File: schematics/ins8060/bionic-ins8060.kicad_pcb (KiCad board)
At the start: 2 copper layers, 48.3 x 71.1 mm, 9 parts, among them J1 Bionic-P135, J2 Bionic-P245, U1 INS8060, U3 11AA010-I/TO

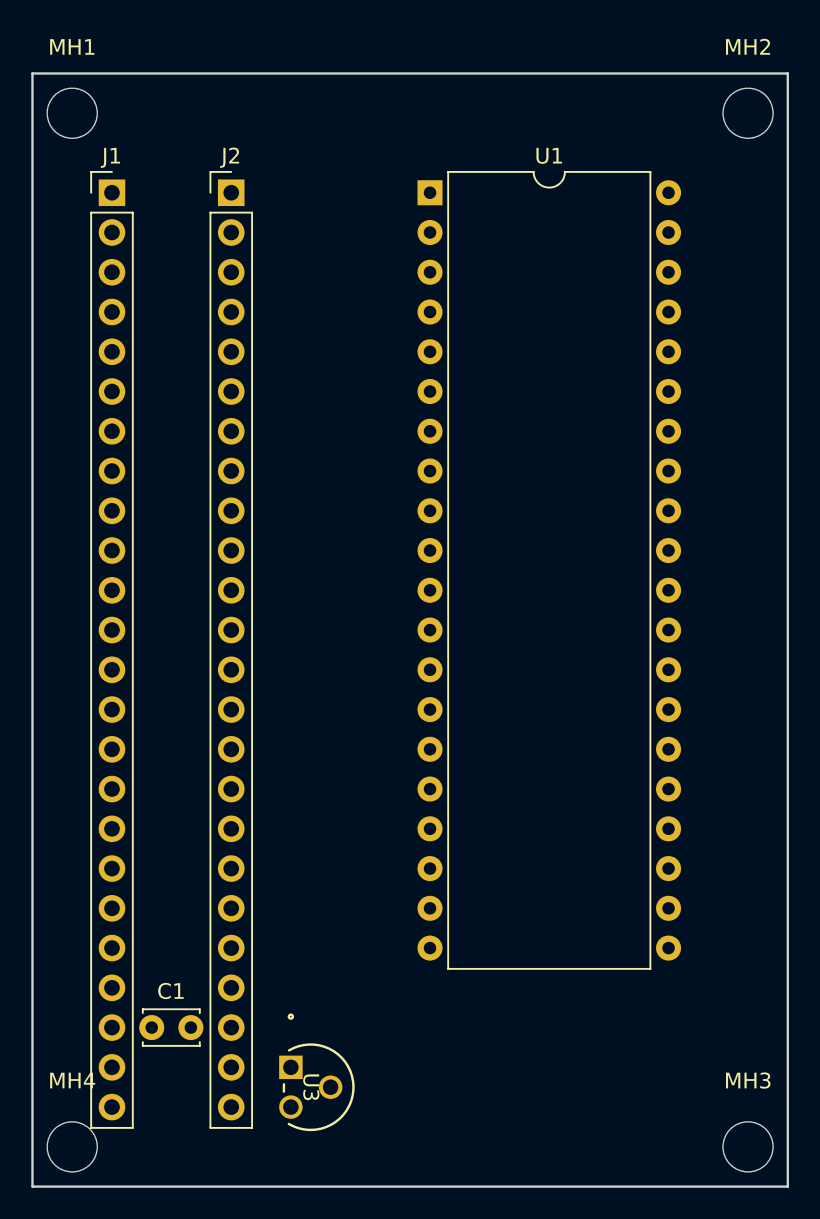
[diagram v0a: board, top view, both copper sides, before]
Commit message: [INS8060] Add power LED
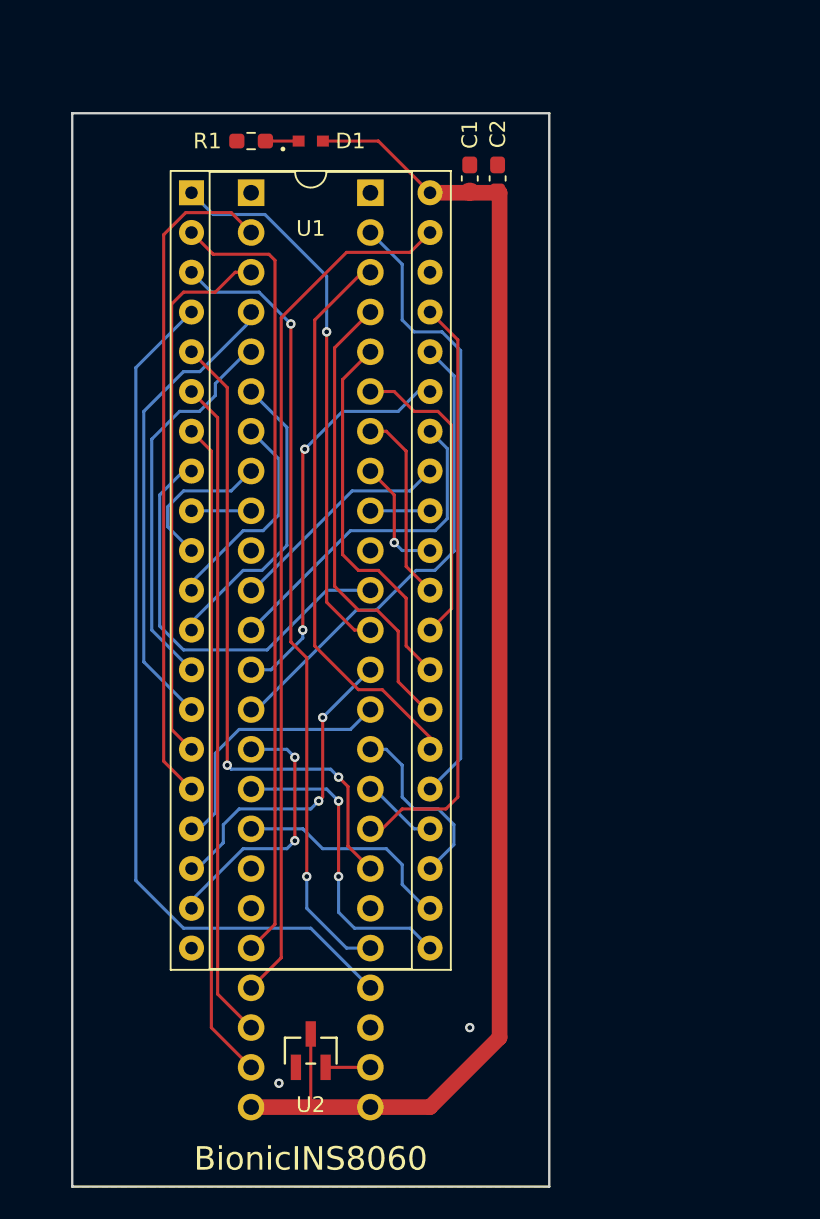
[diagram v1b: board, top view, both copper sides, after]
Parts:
- removed MH1, MH2, MH3, MH4: MountingHole_3.2mm_M3, MountingHole:MountingHole_3.2mm_M3
- removed U3: 11AA010-I/TO, microchip:TO-92_MC_MCH
- added C2: 22u, Capacitor_SMD:C_0603_1608Metric_Pad1.08x0.95mm_HandSolder, F.Cu at (128.2, 74.2)
- added D1: CSL1901UW1, 0-LocalLibrary:LED_CSL1901UW1_ROM, F.Cu at (116.2, 71.8)
- added R1: 1.6k, Resistor_SMD:R_0603_1608Metric_Pad0.98x0.95mm_HandSolder, F.Cu at (112.4, 71.8)
- added U2: 11AA010-I/TT, 0-LocalLibrary:SOT-23_MC_MCH-M, F.Cu at (116.2, 129.9)
- C1: footprint Capacitor_THT:C_Disc_D3.4mm_W2.1mm_P2.50mm -> Capacitor_SMD:C_0603_1608Metric_Pad1.08x0.95mm_HandSolder
- J1: footprint connector:Bionic-P135_Vertical -> 0-LocalLibrary:Bionic-P135_Vertical; moved to B.Cu
- J2: footprint connector:Bionic-P245_Vertical -> 0-LocalLibrary:Bionic-P245_Vertical; moved to B.Cu
- U1: footprint Package_DIP:DIP-40_W15.24mm -> 0-LocalLibrary:DIP-40_W15.24mm_Socket
- moved C1 57.9 mm to (126.4, 74.2), turned to 90 degrees
- moved U1 15.2 mm to (108.6, 75.1)
- moved J1 8.89 mm to (112.4, 75.1), turned to 180 degrees
- moved J2 8.89 mm to (120.0, 75.1), turned to 180 degrees
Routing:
- net VCC: track 0.00 -> 89.4 mm
- net /P55: track 0.00 -> 55.6 mm
- net /P51: track 0.00 -> 55.4 mm
- net /P50: track 0.00 -> 50.9 mm
- net /P54: track 0.00 -> 50.6 mm, vias 0 -> 2
- net /P10: track 0.00 -> 42.9 mm
- net /P53: track 0.00 -> 42.2 mm
- net /P52: track 0.00 -> 42.2 mm
- net /P47: track 0.00 -> 41.5 mm, vias 0 -> 2
- net /P20: track 0.00 -> 39.8 mm
- net /P46: track 0.00 -> 38.2 mm
- net /P21: track 0.00 -> 36.2 mm
- net /P11: track 0.00 -> 36.0 mm
- net /P41: track 0.00 -> 35.2 mm, vias 0 -> 1
- net /P33: track 0.00 -> 30.5 mm
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- added copper zone on B.Cu, net GND
- added copper zone on F.Cu, net GND
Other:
- board size 48.3 x 71.1 mm -> 30.5 x 68.6 mm
- board text added: "BionicINS8060"
- board text added: "Rev. 5"

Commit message: [schematics] Make board edges round
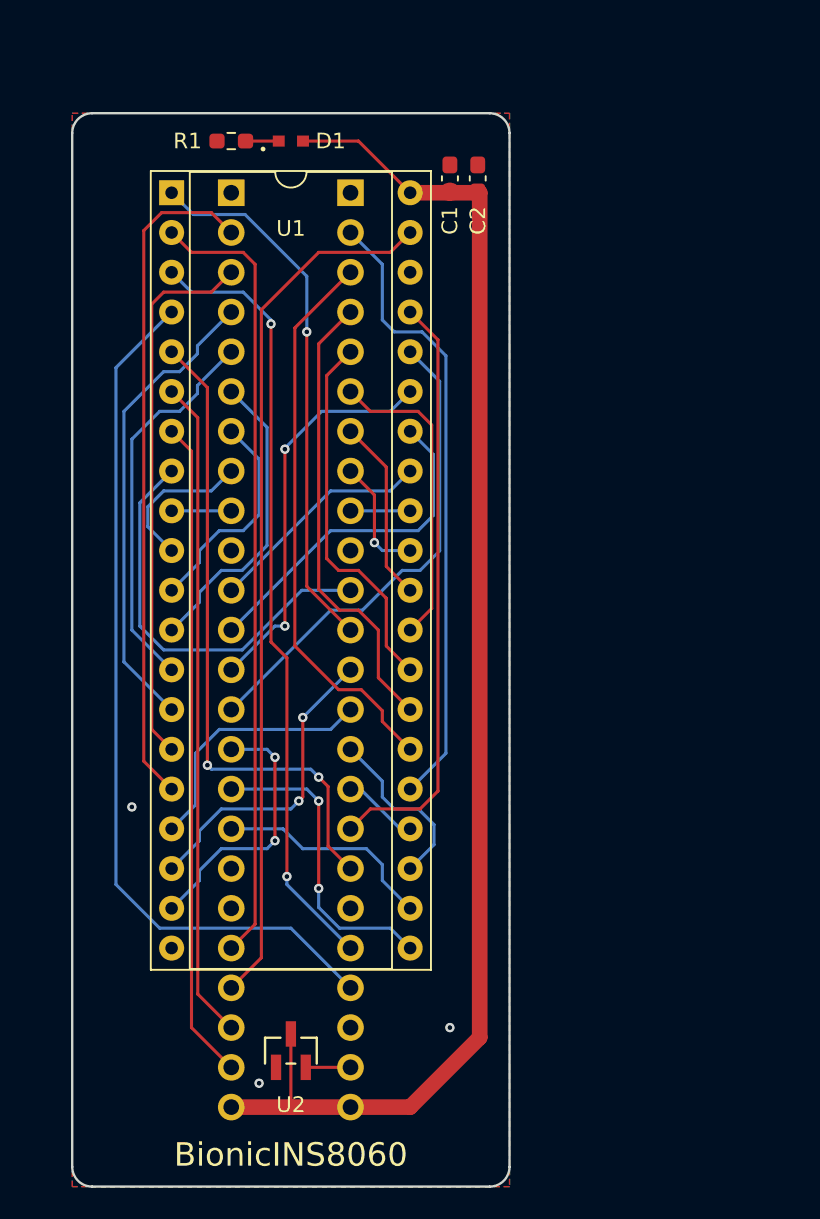
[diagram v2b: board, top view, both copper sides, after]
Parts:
- moved C1 1.27 mm to (125.1, 74.2)
- moved J1 1.27 mm to (111.2, 75.1)
- moved R1 1.27 mm to (111.2, 71.8)
- moved U1 1.27 mm to (107.3, 75.1)
- moved C2 1.27 mm to (126.9, 74.2)
- moved D1 1.27 mm to (115.0, 71.8)
- moved J2 1.27 mm to (118.8, 75.1)
- moved U2 1.27 mm to (115.0, 129.9)
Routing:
- net /P54: track 50.6 -> 49.8 mm
- net /P44: track 12.0 -> 11.4 mm
- net /P25: track 12.3 -> 11.7 mm
- net /P41: track 35.2 -> 34.6 mm
- net GND: vias 2 -> 3
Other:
- board size 30.5 x 68.6 mm -> 27.9 x 68.6 mm
- board text added: "JLCJLCJLCJLC"

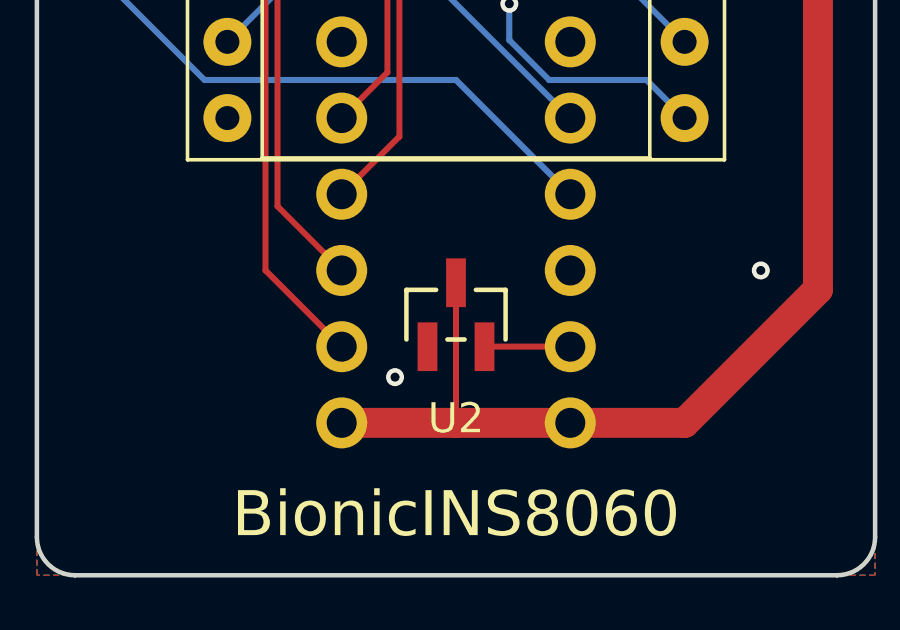
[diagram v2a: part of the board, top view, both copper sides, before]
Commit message: [INS8060] Fix EEPROM pinout
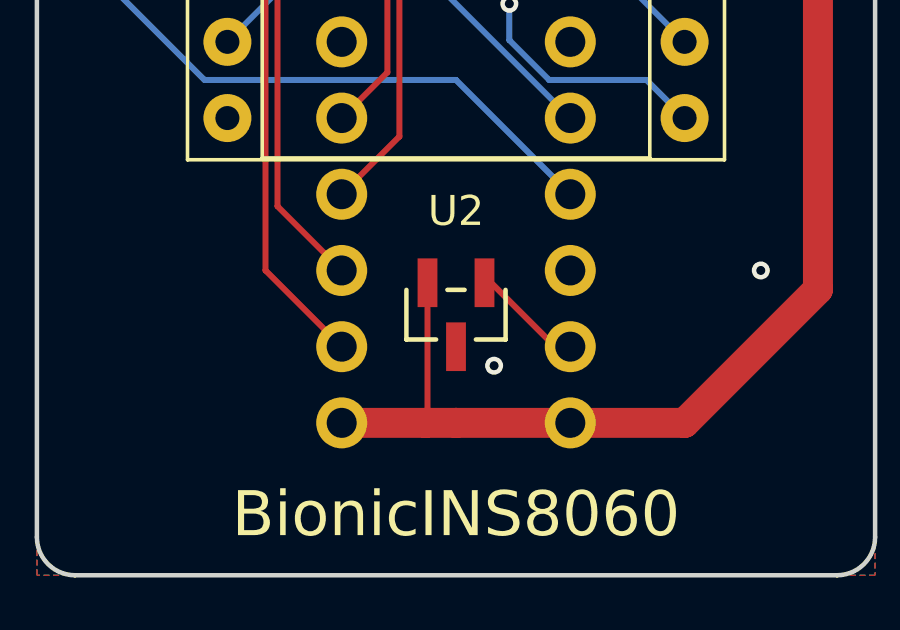
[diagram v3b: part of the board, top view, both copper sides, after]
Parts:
- turned U2 to 180 degrees
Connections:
- U2 pad 1: GND -> Net-(J2-P57)
- U2 pad 2: Net-(J2-P57) -> VCC
- U2 pad 3: VCC -> GND
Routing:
- net Net-(J2-P57): track 2.94 -> 3.74 mm
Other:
- board text added: "Rev. 6"
- board text removed: "Rev. 5"
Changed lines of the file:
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@@
   (title_block
     (title "BionicINS8060")
-    (date "2024-04-24")
-    (rev "5")
+    (date "2024-11-01")
+    (rev "6")
     (company "Tadashi G. Takaoka")
   )
@@
   )
   (footprint "0-LocalLibrary:SOT-23_MC_MCH-M" (layer "F.Cu")
-    (at 114.97 129.894)
+    (at 114.97 129.894 180)
     (descr "Microchip 11AAxxx-I/TT UNI/O 1Kbit Serial EEPROM")
     (property "Sheetfile" "bionic-ins8060.kicad_sch")
@@
         (effects (font (size 1 1) (thickness 0.15)))
     )
-    (fp_text value "11AA010-I/TT" (at 0 0 unlocked) (layer "F.Fab")
+    (fp_text value "11AA010-I/TT" (at 0 0 180 unlocked) (layer "F.Fab")
         (effects (font (size 1 1) (thickness 0.15)))
     )
-    (fp_text user "${REFERENCE}" (at 0 0 unlocked) (layer "F.Fab")
+    (fp_text user "${REFERENCE}" (at 0 0 180 unlocked) (layer "F.Fab")
         (effects (font (size 1 1) (thickness 0.15)))
     )
@@
     (fp_circle (center -1.270999 0.446) (end -1.143999 0.446)
       (stroke (width 0.0254) (type solid)) (fill none) (layer "F.Fab"))
-    (pad "1" smd rect (at -0.950001 1.066) (size 0.6604 1.6256) (layers "F.Cu" "F.Paste" "F.Mask")
+    (pad "1" smd rect (at -0.950001 1.066 180) (size 0.6604 1.6256) (layers "F.Cu" "F.Paste" "F.Mask")
+      (net 43 "Net-(J2-P57)") (pinfunction "SCIO") (pintype "bidirectional"))
+    (pad "2" smd rect (at 0.950001 1.066 180) (size 0.6604 1.6256) (layers "F.Cu" "F.Paste" "F.Mask")
+      (net 1 "VCC") (pinfunction "VCC") (pintype "power_in"))
+    (pad "3" smd rect (at 0 -1.066 180) (size 0.6604 1.6256) (layers "F.Cu" "F.Paste" "F.Mask")
       (net 2 "GND") (pinfunction "VSS") (pintype "power_in"))
-    (pad "2" smd rect (at 0.950001 1.066) (size 0.6604 1.6256) (layers "F.Cu" "F.Paste" "F.Mask")
-      (net 43 "Net-(J2-P57)") (pinfunction "SCIO") (pintype "bidirectional"))
-    (pad "3" smd rect (at 0 -1.066) (size 0.6604 1.6256) (layers "F.Cu" "F.Paste" "F.Mask")
-      (net 1 "VCC") (pinfunction "VCC") (pintype "power_in"))
     (model "${KIPRJMOD}/0-LocalLibrary/SOT-23_MC_MCH.step"
       (offset (xyz 0 0 0))
@@
   (gr_arc (start 102.27 138.58) (mid 101.371974 138.208026) (end 101 137.31)
     (stroke (width 0.15) (type default)) (layer "Edge.Cuts"))
-  (gr_text "Rev. 5" (at 107.096 136.802) (layer "B.SilkS")
+  (gr_text "Rev. 6" (at 107.096 136.802) (layer "B.SilkS")
     (effects (font (size 1 1)) (justify left mirror))
   )
@@
   (segment (start 122.59 133.5) (end 127.035 129.055) (width 1) (layer "F.Cu") (net 1))
   (segment (start 114.97 133.5) (end 118.78 133.5) (width 1) (layer "F.Cu") (net 1))
+  (segment (start 114.019999 128.828) (end 114.019999 133.434001) (width 0.2) (layer "F.Cu") (net 1))
   (segment (start 125.13 75.08) (end 122.59 75.08) (width 1) (layer "F.Cu") (net 1))
-  (segment (start 111.16 133.5) (end 114.97 133.5) (width 1) (layer "F.Cu") (net 1))
-  (segment (start 114.97 133.5) (end 114.97 128.624) (width 0.2) (layer "F.Cu") (net 1))
+  (segment (start 114.019999 133.434001) (end 113.954 133.5) (width 0.2) (layer "F.Cu") (net 1))
   (segment (start 118.78 133.5) (end 122.59 133.5) (width 1) (layer "F.Cu") (net 1))
   (segment (start 125.13 75.08) (end 125.13 74.9265) (width 1) (layer "F.Cu") (net 1))
   (segment (start 119.288 71.778) (end 122.59 75.08) (width 0.2) (layer "F.Cu") (net 1))
+  (segment (start 111.16 133.5) (end 113.954 133.5) (width 1) (layer "F.Cu") (net 1))
   (segment (start 115.7447 71.778) (end 119.288 71.778) (width 0.2) (layer "F.Cu") (net 1))
   (segment (start 127.035 75.08) (end 125.13 75.08) (width 1) (layer "F.Cu") (net 1))
+  (segment (start 113.954 133.5) (end 114.97 133.5) (width 1) (layer "F.Cu") (net 1))
   (segment (start 127.035 129.055) (end 127.035 75.08) (width 1) (layer "F.Cu") (net 1))
-  (via (at 112.938 131.976) (size 0.6) (drill 0.3) (layers "F.Cu" "B.Cu") (free) (net 2))
   (via (at 125.13 128.42) (size 0.6) (drill 0.3) (layers "F.Cu" "B.Cu") (free) (net 2))
+  (via (at 116.24 131.595) (size 0.6) (drill 0.3) (layers "F.Cu" "B.Cu") (free) (net 2))
   (via (at 104.81 114.323) (size 0.6) (drill 0.3) (layers "F.Cu" "B.Cu") (free) (net 2))
   (segment (start 108.62 91.59) (end 107.35 90.32) (width 0.2) (layer "F.Cu") (net 3))
@@
   (segment (start 107.35 77.62) (end 108.62 78.89) (width 0.2) (layer "F.Cu") (net 39))
   (segment (start 112.684 121.816) (end 111.16 123.34) (width 0.2) (layer "F.Cu") (net 39))
-  (segment (start 118.78 130.96) (end 116.124 130.96) (width 0.2) (layer "F.Cu") (net 43))
-  (segment (start 116.124 130.96) (end 115.92 130.756) (width 0.2) (layer "F.Cu") (net 43))
+  (segment (start 116.14 128.828) (end 118.272 130.96) (width 0.2) (layer "F.Cu") (net 43))
+  (segment (start 118.272 130.96) (end 118.78 130.96) (width 0.2) (layer "F.Cu") (net 43))
+  (segment (start 115.920001 128.828) (end 116.14 128.828) (width 0.2) (layer "F.Cu") (net 43))
   (segment (start 114.1953 71.778) (end 112.0725 71.778) (width 0.2) (layer "F.Cu") (net 48))
   (zone (net 2) (net_name "GND") (layers "F&B.Cu") (hatch edge 0.5)

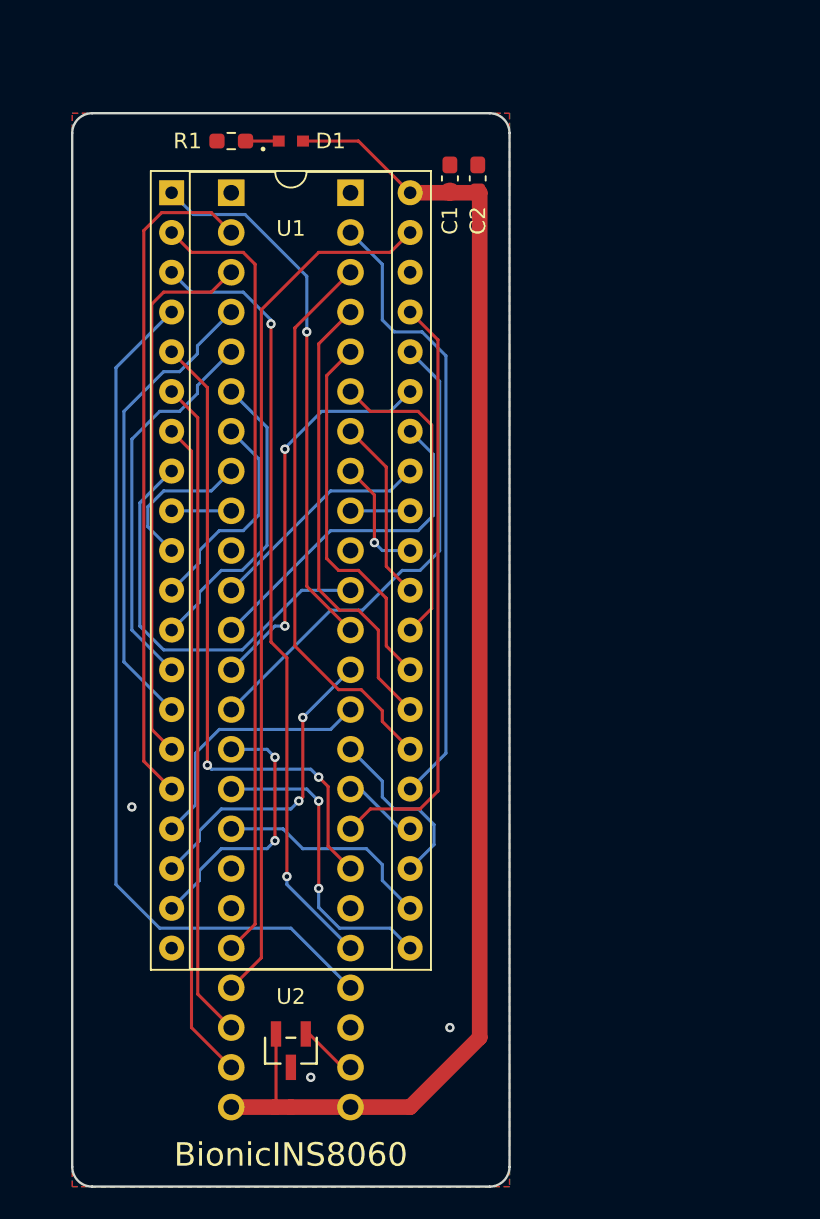
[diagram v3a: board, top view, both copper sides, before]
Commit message: [INS8060] Shrink board size
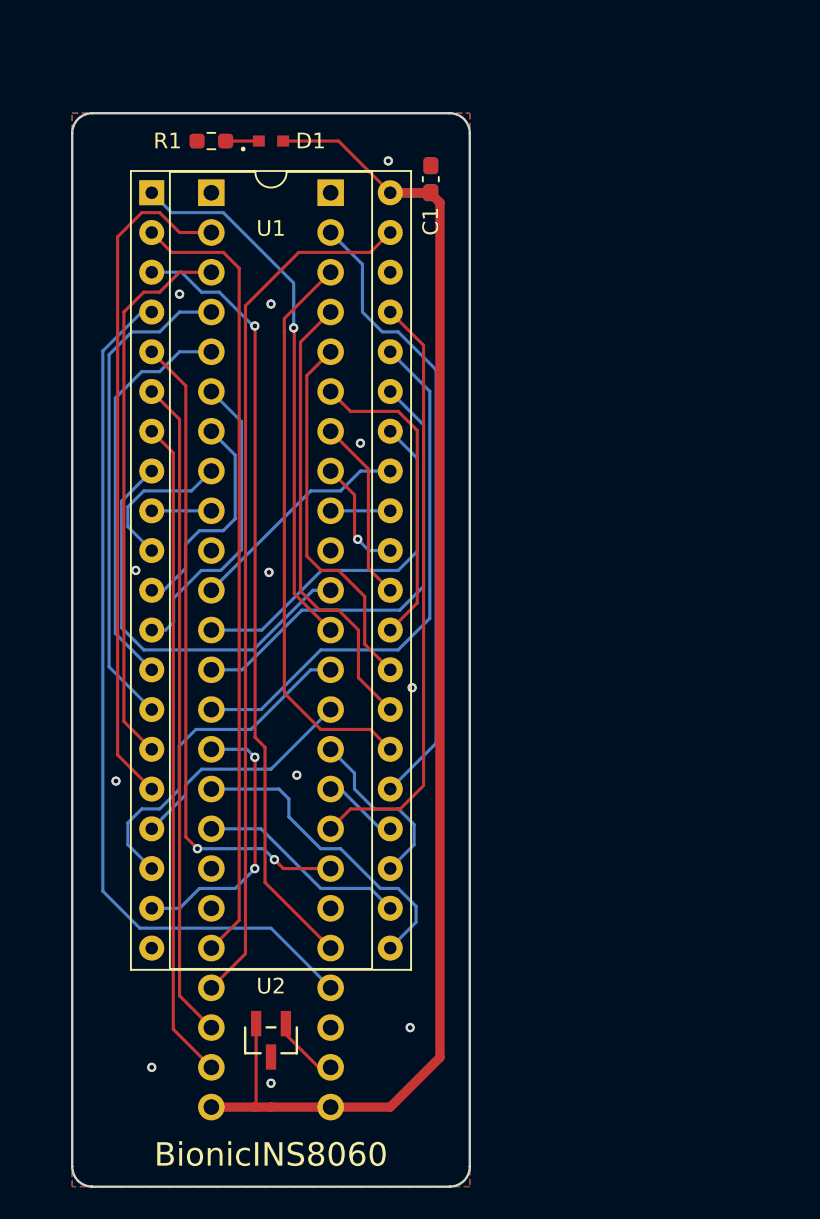
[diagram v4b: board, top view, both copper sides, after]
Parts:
- C2: moved to B.Cu
- moved C2 3.00 mm to (123.9, 74.2)
- moved U2 1.43 mm to (113.7, 129.2)
- moved D1 1.27 mm to (113.7, 71.8)
- moved J1 1.27 mm to (109.9, 75.1)
- moved J2 1.27 mm to (117.5, 75.1)
- moved R1 1.27 mm to (109.9, 71.8)
- moved U1 1.27 mm to (106.1, 75.1)
- moved C1 1.22 mm to (123.9, 74.2)
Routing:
- net /P32: track 25.5 -> 29.1 mm, vias 2 -> 0
- net /P33: track 31.0 -> 34.4 mm
- net /P42: track 20.0 -> 22.2 mm, vias 2 -> 0
- net /P31: track 21.9 -> 23.6 mm
- net /P43: track 16.5 -> 15.0 mm
- net /P12: track 30.1 -> 31.5 mm
- net /P13: track 24.7 -> 25.7 mm
- net VCC: track 89.2 -> 90.1 mm
- net Net-(J2-P57): track 3.74 -> 4.43 mm
- net /P34: track 17.1 -> 17.8 mm
- net /P36: track 14.1 -> 13.5 mm
- net /P35: track 19.6 -> 20.2 mm, vias 2 -> 0
- net /P47: track 41.5 -> 42.0 mm
- net /P21: track 35.9 -> 36.4 mm
- net /P54: vias 2 -> 1
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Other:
- board size 27.9 x 68.6 mm -> 25.4 x 68.6 mm
